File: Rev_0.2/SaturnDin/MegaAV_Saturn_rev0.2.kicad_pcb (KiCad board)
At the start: 2 copper layers, 40.4 x 55 mm, 151 parts, among them CN1 MD-90SM_MD2, P1 SMD_Conn_01x01, U1 ICS501, U2 MC33204, U3 THS7374, U4 MC33204, U5 AD725

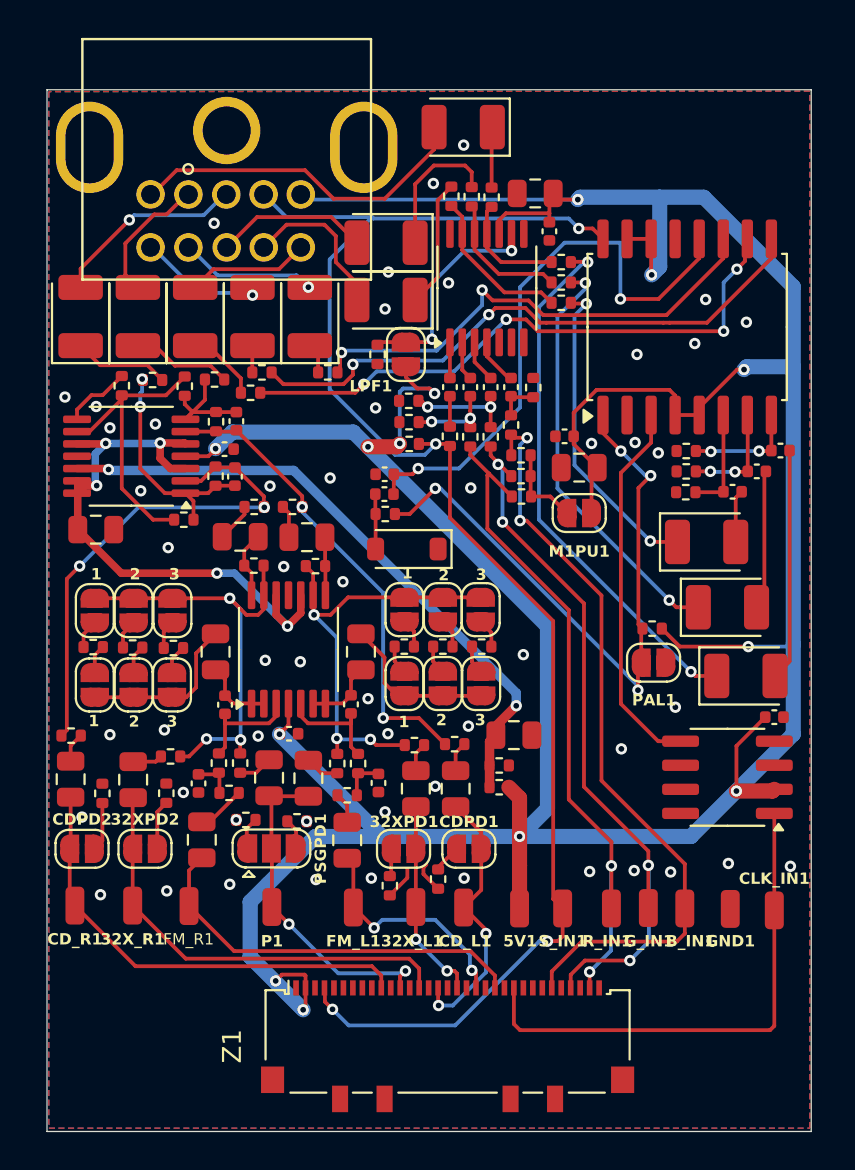
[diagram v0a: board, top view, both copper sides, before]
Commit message: fixed silkscreening, minor trace rerouting, and added PCBA files. Note, these are not final.
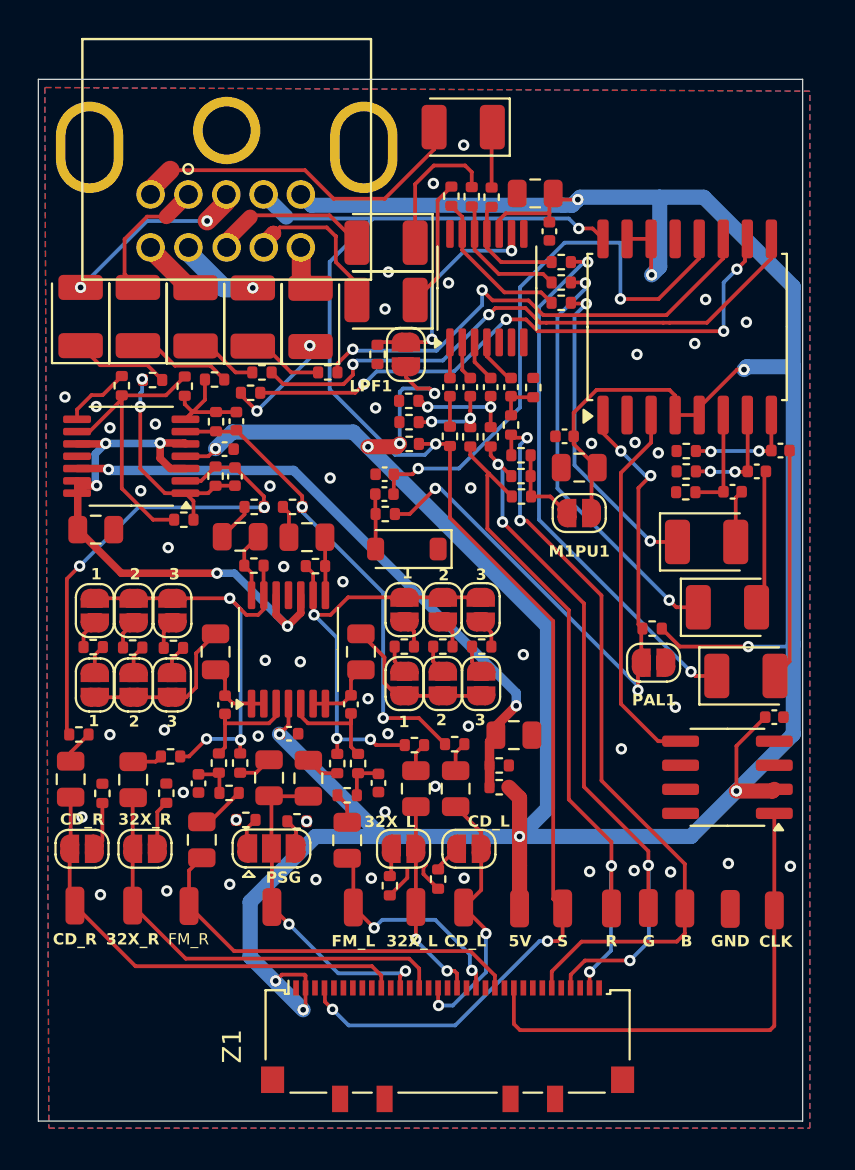
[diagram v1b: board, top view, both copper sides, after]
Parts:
- moved C44 6.09 mm to (236.7, 114.2)
- moved C42 3.01 mm to (233.7, 114.2)
- moved C43 3.01 mm to (230.7, 114.1)
- moved R38 0.41 mm to (224.5, 136.2)
- renumbered 32X_L1 to 32X_L, 32XPD1 to 32X_L, 32X_R1 to 32X_R, 32XPD2 to 32X_R, 5V1 to 5V, B_IN1 to B, CD_L1 to CD_L, CDPD1 to CD_L, CDPD2 to CD_R, CD_R1 to CD_R, CLK_IN1 to CLK, FM_L1 to FM_L, FM_R1 to FM_R, G_IN1 to G, GND1 to GND, PSGPD1 to PSG, R_IN1 to R, S_IN1 to S
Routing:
- net /CV-OUT: track 6.51 -> 2.51 mm
- net Net-(C43-Pad1): track 1.54 -> 5.31 mm
- net /C-OUT: track 6.32 -> 3.31 mm, vias 1 -> 0
- net /Y-OUT: track 7.22 -> 4.44 mm
- net Net-(C42-Pad1): track 1.59 -> 4.04 mm
- net Net-(C44-Pad1): track 4.94 -> 5.97 mm, vias 0 -> 2
- net /AUD-R: track 10.2 -> 9.95 mm, vias 1 -> 2
- net GND: vias 53 -> 52

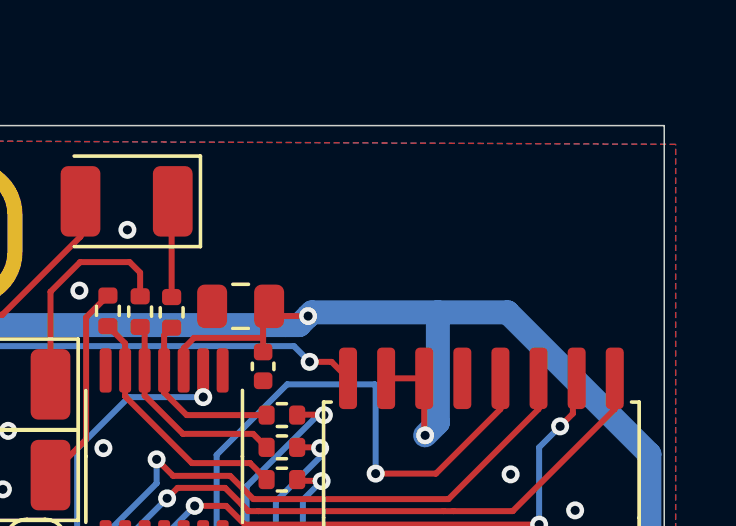
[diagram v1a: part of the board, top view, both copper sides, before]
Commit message: Added MegaAV logo
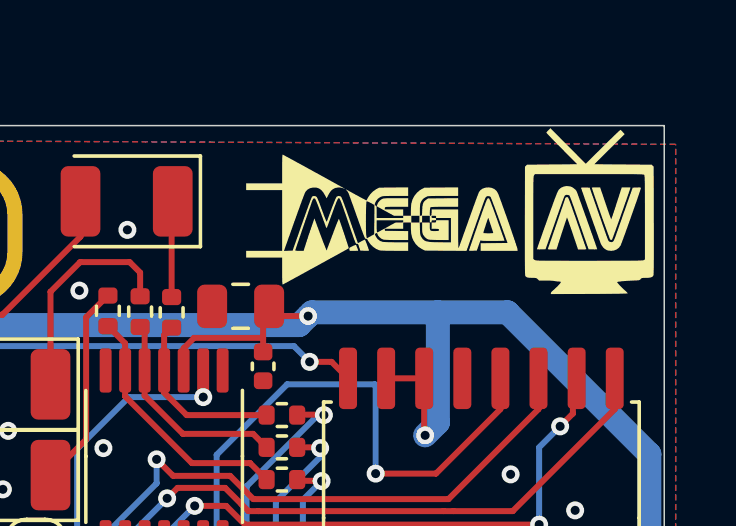
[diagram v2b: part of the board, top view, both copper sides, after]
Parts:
- added G***: LOGO, LOGO_Library:MegaAV Logo (Small), F.Cu at (256.0, 104.2)
- added G***: LOGO, LOGO_Library:MegaAV Logo 2, B.Cu at (242.2, 146.9)
